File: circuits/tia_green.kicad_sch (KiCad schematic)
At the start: 11 parts, among them U3 OPA380AID

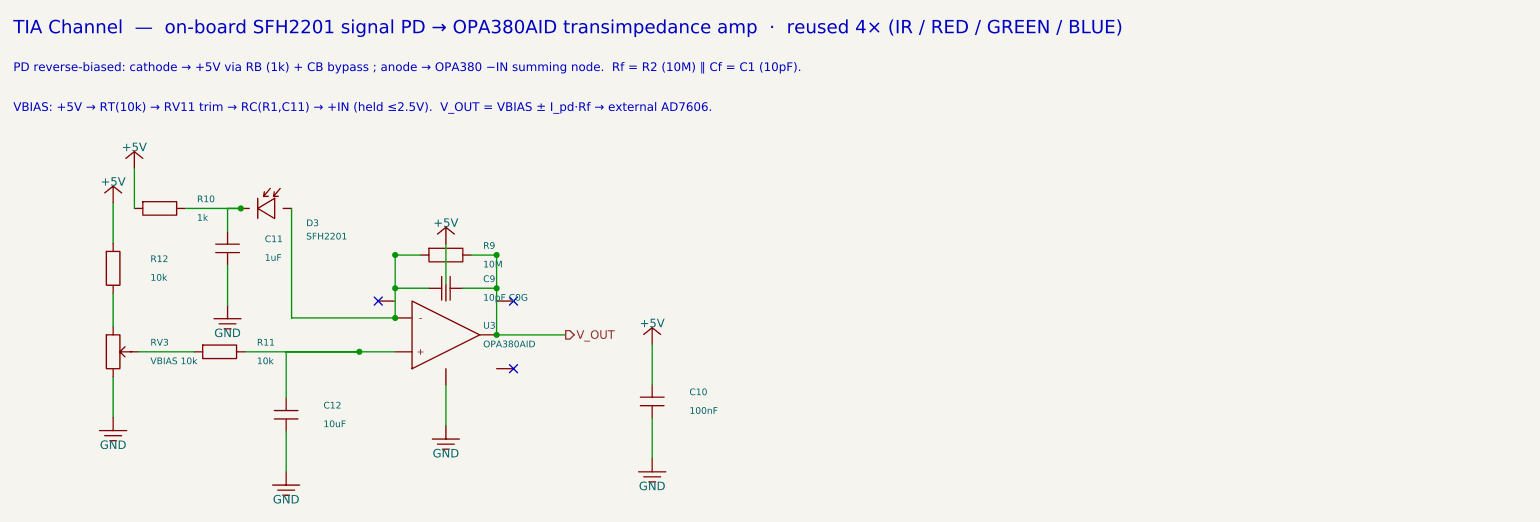
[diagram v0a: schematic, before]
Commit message: fix(circuits): import mcu sheet and laser footprints
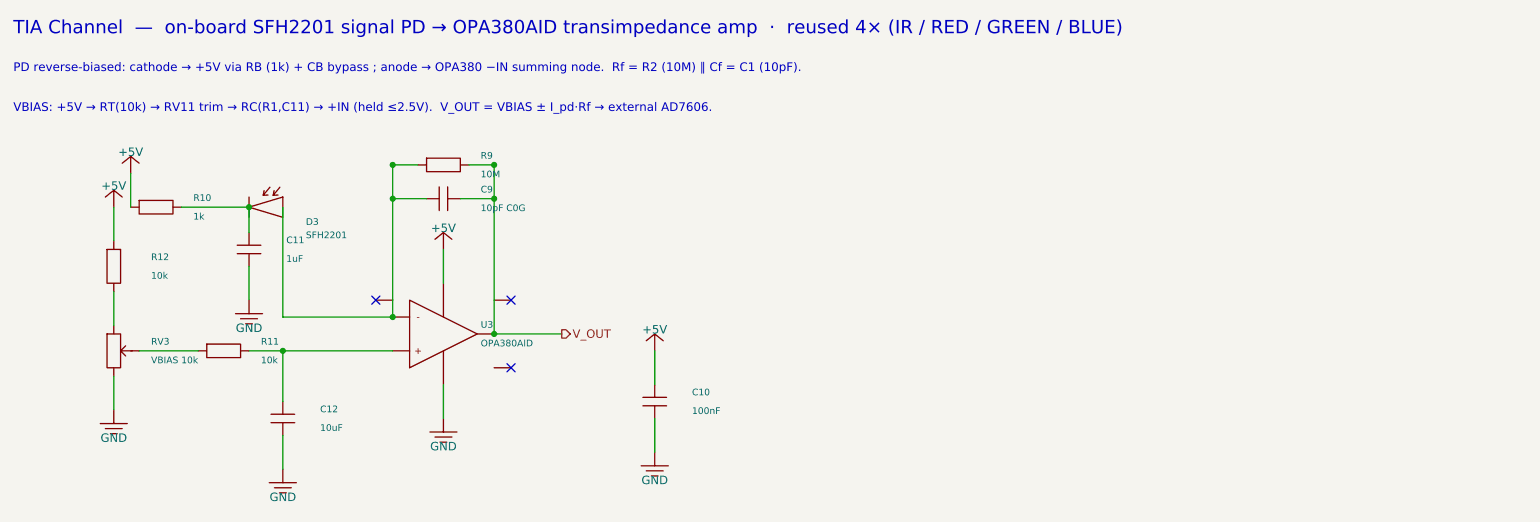
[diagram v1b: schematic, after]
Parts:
- removed R11: 10k, Resistor_SMD:R_0603_1608Metric_Pad0.98x0.95mm_HandSolder, symbol viv:R_H
- added RV3: VBIAS 10k, Potentiometer_SMD:Potentiometer_Bourns_3224W_Vertical, symbol viv:POT_V
- C10: LCSC C1525 -> C83056; Part Number CL05B104KO5NNNC -> 0402B104K160CT
- C11: LCSC C52923 -> C7472946; Part Number CL05A105KA5NQNC -> HGC0402R5105K250NTEJ
- C12: LCSC C15850 -> C318691; Part Number CL21A106KAYNNNE -> CL21A106KAYNNNG
- R10: LCSC C21190 -> C2907002; Part Number 0603WAF1001T5E -> FRC0603F1001TS
- R11: renamed from RV3; value VBIAS 10k -> 10k; footprint Potentiometer_SMD:Potentiometer_Bourns_3224W_Vertical -> Resistor_SMD:R_0603_1608Metric_Pad0.98x0.95mm_HandSolder; symbol viv:POT_V -> viv:R_H; LCSC C81348 -> C844918; Part Number 3224W-1-103E -> CRCW060310K0FKEA
- R12: LCSC C269701 -> C844918; Part Number 0603WAF1002T5E -> CRCW060310K0FKEA
- R9: LCSC C57129 -> C844730; Part Number 0603WAF1005T5E -> CRCW060310M0FKEA
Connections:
- net GND: now also RV3.3; no longer R11.3
- net at C12.1, U3.3 (+): now also R11.2
- net at R12.2: now also RV3.1; no longer R11.1
- new net: R11.1, RV3.2 (W)

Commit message: save laser controller schematic and layout state
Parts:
- removed D3: SFH2201, OptoDevice:Osram_SFH2201, symbol viv:PHOTODIODE
- removed R10: 1k, Resistor_SMD:R_0603_1608Metric_Pad0.98x0.95mm_HandSolder, symbol viv:R_H
- removed R9: 10M, Resistor_SMD:R_0603_1608Metric_Pad0.98x0.95mm_HandSolder, symbol viv:R_H
- removed RV3: VBIAS 10k, Potentiometer_SMD:Potentiometer_Bourns_3224W_Vertical, symbol viv:POT_V
- added C11: 1uF, Capacitor_SMD:C_0402_1005Metric_Pad0.74x0.62mm_HandSolder, symbol viv:C_V
- added C12: 10uF, Capacitor_SMD:C_0805_2012Metric_Pad1.18x1.45mm_HandSolder, symbol viv:C_V
- added R11: 10k, Resistor_SMD:R_0603_1608Metric_Pad0.98x0.95mm_HandSolder, symbol viv:R_H
- added U3: OPA380AID, Package_SO:SOIC-8_3.9x4.9mm_P1.27mm, symbol viv:OPA_N
- D3: renamed from C11; value 1uF -> SFH2201; footprint Capacitor_SMD:C_0402_1005Metric_Pad0.74x0.62mm_HandSolder -> OptoDevice:Osram_SFH2201; symbol viv:C_V -> viv:PHOTODIODE; LCSC C7472946 -> C2900216; Part Number HGC0402R5105K250NTEJ -> SFH2201
- R10: renamed from U3; value OPA380AID -> 1k; footprint Package_SO:SOIC-8_3.9x4.9mm_P1.27mm -> Resistor_SMD:R_0603_1608Metric_Pad0.98x0.95mm_HandSolder; symbol viv:OPA_N -> viv:R_H; LCSC C201677 -> C2907002; Part Number OPA380AID -> FRC0603F1001TS
- R12: renamed from R11; symbol viv:R_H -> viv:R_V
- RV3: renamed from C12; value 10uF -> VBIAS 10k; footprint Capacitor_SMD:C_0805_2012Metric_Pad1.18x1.45mm_HandSolder -> Potentiometer_SMD:Potentiometer_Bourns_3224W_Vertical; symbol viv:C_V -> viv:POT_V; LCSC C318691 -> C81348; Part Number CL21A106KAYNNNG -> 3224W-1-103E
- RV7: renamed from R12; value 10k -> RF 2M; footprint Resistor_SMD:R_0603_1608Metric_Pad0.98x0.95mm_HandSolder -> Potentiometer_SMD:Potentiometer_Bourns_3224W_Vertical; symbol viv:R_V -> viv:POT_H; LCSC C844918 -> C116323; Part Number CRCW060310K0FKEA -> 3224W-1-205E
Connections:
- net +5V: now also R10.1, R12.1, U3.7 (V+); no longer R10.7 (V+), RV7.1
- net GND: now also RV3.3, C11.2, C12.2, U3.4 (V-); no longer D3.2, R10.4 (V-), RV3.2
- net V_OUT: now also RV7.2 (W), RV7.3, U3.6; no longer R10.6
- net at D3.1 (K): now also R10.2, C11.1
- net at C9.1: now also D3.2 (A), RV7.1, U3.2 (-); no longer R10.2 (-)
- net at R12.2, RV3.1: no longer R10.3 (+)
- new net: C12.1, R11.2, U3.3 (+)
- new net: R11.1, RV3.2 (W)
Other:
- note added: "PD reverse-biased: cathode → +5V via RB (1k) + CB bypass ; anode → OPA380 −IN summing node. Rf = RVFB (2M trim) ∥ Cf = C1 (10pF)."
- note added: "VBIAS: +5V → RT(10k) → RV11 trim → RC(R1,C11) → +IN (held ≤2.5V). V_OUT = VBIAS ± I_pd·Rf → on-board AD7606-4."
- note removed: "PD reverse-biased: cathode → +5V via RB (1k) + CB bypass ; anode → OPA380 −IN summing node. Rf = R2 (10M) ∥ Cf = C1 (10pF)."
- note removed: "VBIAS: +5V → RT(10k) → RV11 trim → RC(R1,C11) → +IN (held ≤2.5V). V_OUT = VBIAS ± I_pd·Rf → external AD7606."
- moved on the sheet: R12
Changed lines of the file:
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@@
     )
   )
-  (symbol (lib_id "viv:R_H") (at 214.63 124.46 0) (unit 1)
-    (in_bom yes) (on_board yes) (dnp no)
-    (property "Reference" "R9" (at 220.23 123.06 0) (effects (font (size 1.0 1.0)) (justify left)))
-    (property "Value" "10M" (at 220.23 125.86 0) (effects (font (size 1.0 1.0)) (justify left)))
-    (property "Footprint" "Resistor_SMD:R_0603_1608Metric_Pad0.98x0.95mm_HandSolder" (at 214.63 124.46 0) (effects (font (size 1.0 1.0)) hide))
+  (symbol (lib_id "viv:POT_H") (at 214.63 124.46 0) (unit 1)
+    (in_bom yes) (on_board yes) (dnp no)
+    (property "Reference" "RV7" (at 220.23 123.06 0) (effects (font (size 1.0 1.0)) (justify left)))
+    (property "Value" "RF 2M" (at 220.23 125.86 0) (effects (font (size 1.0 1.0)) (justify left)))
+    (property "Footprint" "Potentiometer_SMD:Potentiometer_Bourns_3224W_Vertical" (at 214.63 124.46 0) (effects (font (size 1.0 1.0)) hide))
     (property "Datasheet" "" (at 214.63 124.46 0) (effects (font (size 1.0 1.0)) hide))
-    (property "Part Number" "CRCW060310M0FKEA" (at 214.63 124.46 0) (effects (font (size 1.0 1.0)) hide))
-    (property "LCSC" "C844730" (at 214.63 124.46 0) (effects (font (size 1.0 1.0)) hide))
-    (pin "1")
-    (pin "2")
-    (instances
-      (project "laser_controller"
-        (path "/c1d2e3f4-6000-4000-a000-000000000001" (reference "R9") (unit 1))
+    (property "Part Number" "3224W-1-205E" (at 214.63 124.46 0) (effects (font (size 1.0 1.0)) hide))
+    (property "LCSC" "C116323" (at 214.63 124.46 0) (effects (font (size 1.0 1.0)) hide))
+    (pin "1")
+    (pin "2")
+    (pin "3")
+    (instances
+      (project "laser_controller"
+        (path "/c1d2e3f4-6000-4000-a000-000000000001" (reference "RV7") (unit 1))
       )
     )
@@
   (wire (pts (xy 210.82 124.46) (xy 207.01 124.46)) (stroke (width 0) (type default)))
   (wire (pts (xy 218.44 124.46) (xy 222.25 124.46)) (stroke (width 0) (type default)))
+  (wire (pts (xy 214.63 120.65) (xy 222.25 120.65)) (stroke (width 0) (type default)))
+  (wire (pts (xy 222.25 120.65) (xy 222.25 124.46)) (stroke (width 0) (type default)))
   (wire (pts (xy 212.09 129.54) (xy 207.01 129.54)) (stroke (width 0) (type default)))
   (wire (pts (xy 217.17 129.54) (xy 222.25 129.54)) (stroke (width 0) (type default)))
@@
   (hierarchical_label "V_OUT" (shape output) (at 232.41 149.86 0) (effects (font (size 1.27 1.27)) (justify left)))
   (text "TIA Channel  —  on-board SFH2201 signal PD → OPA380AID transimpedance amp  ·  reused 4× (IR / RED / GREEN / BLUE)" (at 150 104 0) (effects (font (size 2.0 2.0)) (justify left)))
-  (text "PD reverse-biased: cathode → +5V via RB (1k) + CB bypass ; anode → OPA380 −IN summing node.  Rf = R2 (10M) ∥ Cf = C1 (10pF)." (at 150 110 0) (effects (font (size 1.3 1.3)) (justify left)))
-  (text "VBIAS: +5V → RT(10k) → RV11 trim → RC(R1,C11) → +IN (held ≤2.5V).  V_OUT = VBIAS ± I_pd·Rf → external AD7606." (at 150 116 0) (effects (font (size 1.3 1.3)) (justify left)))
+  (text "PD reverse-biased: cathode → +5V via RB (1k) + CB bypass ; anode → OPA380 −IN summing node.  Rf = RVFB (2M trim) ∥ Cf = C1 (10pF)." (at 150 110 0) (effects (font (size 1.3 1.3)) (justify left)))
+  (text "VBIAS: +5V → RT(10k) → RV11 trim → RC(R1,C11) → +IN (held ≤2.5V).  V_OUT = VBIAS ± I_pd·Rf → on-board AD7606-4." (at 150 116 0) (effects (font (size 1.3 1.3)) (justify left)))
   (sheet_instances
     (path "/" (page "1"))
